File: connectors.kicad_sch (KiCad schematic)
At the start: 1 part

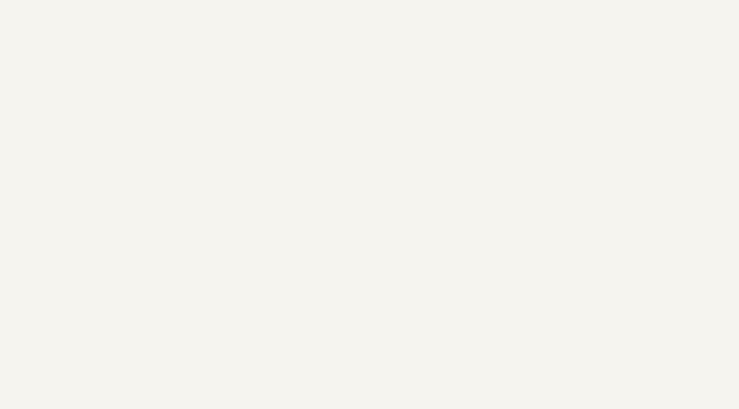
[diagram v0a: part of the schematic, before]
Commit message: Add FAKRA connector
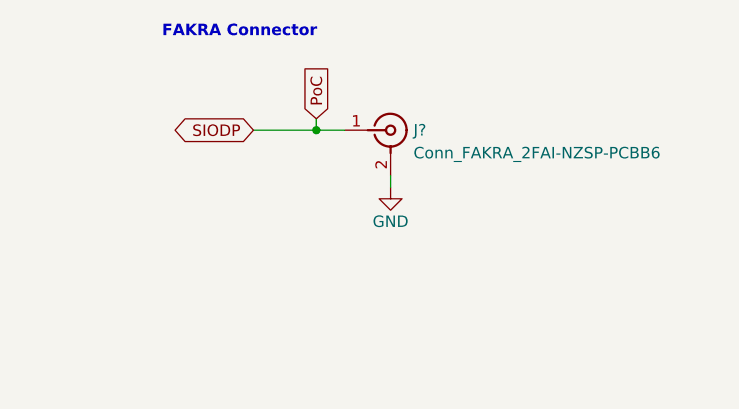
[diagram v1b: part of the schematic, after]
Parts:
- added J?: Conn_FAKRA_2FAI-NZSP-PCBB6, antmicro-footprints:Conn_FAKRA_59S2AQ-40MT5-Z_1, symbol antmicroCoaxialConnectorsRF:Conn_FAKRA_59S2AQ-40MT5-Z_1
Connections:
- net GND: now also J?.2, J?.3, J?.4, J?.5
- new net PoC: J?.1
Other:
- note added: "FAKRA Connector"
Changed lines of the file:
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@@
   (junction (at 58.42 68.58) (diameter 0) (color 0 0 0 0)
+  )
+  (junction (at 230.505 40.64) (diameter 0) (color 0 0 0 0)
   )
   (junction (at 62.23 157.48) (diameter 0) (color 0 0 0 0)
@@
     (stroke (width 0) (type default) (color 0 0 0 0))
   )
+  (wire (pts (xy 230.505 40.64) (xy 233.68 40.64))
+    (stroke (width 0) (type default) (color 0 0 0 0))
+  )
   (wire (pts (xy 52.07 160.02) (xy 62.23 160.02))
     (stroke (width 0) (type default) (color 0 0 0 0))
@@
     (stroke (width 0) (type default) (color 0 0 0 0))
   )
+  (wire (pts (xy 238.76 45.72) (xy 238.76 46.99))
+    (stroke (width 0) (type default) (color 0 0 0 0))
+  )
+  (wire (pts (xy 230.505 39.37) (xy 230.505 40.64))
+    (stroke (width 0) (type default) (color 0 0 0 0))
+  )
   (wire (pts (xy 62.23 157.48) (xy 62.23 160.02))
     (stroke (width 0) (type default) (color 0 0 0 0))
@@
   )
   (wire (pts (xy 52.07 139.7) (xy 64.77 139.7))
+    (stroke (width 0) (type default) (color 0 0 0 0))
+  )
+  (wire (pts (xy 223.52 40.64) (xy 230.505 40.64))
     (stroke (width 0) (type default) (color 0 0 0 0))
   )
@@
     (effects (font (size 1.27 1.27)) (justify left bottom))
   )
+  (text "FAKRA Connector\n" (at 213.36 30.48 0)
+    (effects (font (size 1.27 1.27) (thickness 0.254) bold) (justify left bottom))
+  )
   (text "FFC CSI Connector" (at 38.1 30.48 0)
     (effects (font (size 1.27 1.27) (thickness 0.254) bold) (justify left bottom))
@@
     )
   )
+  (global_label "PoC" (shape input) (at 230.505 39.37 90) (fields_autoplaced)
+    (effects (font (size 1.27 1.27)) (justify left))
+    (property "Intersheet References" "${INTERSHEET_REFS}" (id 0) (at 230.4256 33.2679 90)
+      (effects (font (size 1.27 1.27)) (justify left) hide)
+    )
+  )
   (global_label "CSI0_CLK_N" (shape input) (at 64.77 109.22 0) (fields_autoplaced)
     (effects (font (size 1.27 1.27)) (justify left))
@@
     (property "Intersheet References" "${INTERSHEET_REFS}" (id 0) (at 72.8679 139.6206 0)
       (effects (font (size 1.27 1.27)) (justify left) hide)
+    )
+  )
+  (global_label "SIODP" (shape bidirectional) (at 223.52 40.64 180)
+    (effects (font (size 1.27 1.27)) (justify right))
+    (property "Intersheet References" "${INTERSHEET_REFS}" (id 0) (at 213.36 40.64 0)
+      (effects (font (size 1.27 1.27)) (justify right) hide)
     )
   )
@@
     )
     (pin "1")
+  )
+  (symbol (lib_id "antmicroCoaxialConnectorsRF:Conn_FAKRA_59S2AQ-40MT5-Z_1") (at 233.68 40.64 0) (unit 1)
+    (in_bom yes) (on_board yes)
+    (property "Reference" "J?" (id 0) (at 241.3 40.64 0)
+      (effects (font (size 1.27 1.27) (thickness 0.15)) (justify left))
+    )
+    (property "Value" "Conn_FAKRA_2FAI-NZSP-PCBB6" (id 1) (at 241.3 43.18 0)
+      (effects (font (size 1.27 1.27) (thickness 0.15)) (justify left))
+    )
+    (property "Footprint" "antmicro-footprints:Conn_FAKRA_59S2AQ-40MT5-Z_1" (id 2) (at 254 50.8 0)
+      (effects (font (size 1.27 1.27) (thickness 0.15)) (justify left bottom) hide)
+    )
+    (property "Datasheet" "https://products.rosenberger.com/radio-frequency/connectors/288881/59s2aq-40mt5-z-1-right-angle-plug-pcb-w.-housing" (id 3) (at 254 53.34 0)
+      (effects (font (size 1.27 1.27) (thickness 0.15)) (justify left bottom) hide)
+    )
+    (property "MPN" "59S2AQ-40MT5-Z_1" (id 4) (at 254 55.88 0)
+      (effects (font (size 1.27 1.27) (thickness 0.15)) (justify left bottom) hide)
+    )
+    (property "Manufacturer" "Rosenberger" (id 5) (at 254 58.42 0)
+      (effects (font (size 1.27 1.27) (thickness 0.15)) (justify left bottom) hide)
+    )
+    (property "Author" "Antmicro" (id 6) (at 254 60.96 0)
+      (effects (font (size 1.27 1.27) (thickness 0.15)) (justify left bottom) hide)
+    )
+    (property "License" "Apache-2.0" (id 7) (at 254 63.5 0)
+      (effects (font (size 1.27 1.27) (thickness 0.15)) (justify left bottom) hide)
+    )
+    (pin "1")
+    (pin "2")
+    (pin "3")
+    (pin "4")
+    (pin "5")
   )
   (symbol (lib_id "antmicroFCCConnectors:Conn_FFC_WE_68715014022") (at 52.07 40.64 0) (mirror y) (unit 1)
@@
     (pin "MP2")
   )
+  (symbol (lib_id "antmicropower:GND") (at 238.76 46.99 0) (unit 1)
+    (in_bom yes) (on_board yes)
+    (property "Reference" "#PWR?" (id 0) (at 247.65 49.53 0)
+      (effects (font (size 1.27 1.27) (thickness 0.15)) (justify left bottom) hide)
+    )
+    (property "Value" "GND" (id 1) (at 238.76 50.8 0)
+      (effects (font (size 1.27 1.27) (thickness 0.15)))
+    )
+    (property "Footprint" "" (id 2) (at 247.65 54.61 0)
+      (effects (font (size 1.27 1.27) (thickness 0.15)) (justify left bottom) hide)
+    )
+    (property "Datasheet" "" (id 3) (at 247.65 59.69 0)
+      (effects (font (size 1.27 1.27) (thickness 0.15)) (justify left bottom) hide)
+    )
+    (property "Author" "Antmicro" (id 4) (at 247.65 54.61 0)
+      (effects (font (size 1.27 1.27) (thickness 0.15)) (justify left bottom) hide)
+    )
+    (property "License" "Apache-2.0" (id 5) (at 247.65 57.15 0)
+      (effects (font (size 1.27 1.27) (thickness 0.15)) (justify left bottom) hide)
+    )
+    (pin "1")
+  )
 )

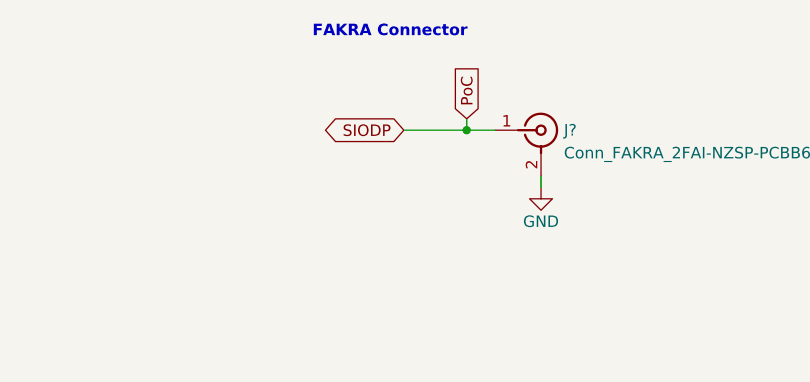
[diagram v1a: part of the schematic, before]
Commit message: [WiP]:Add serializer signals and decoupling capacitors
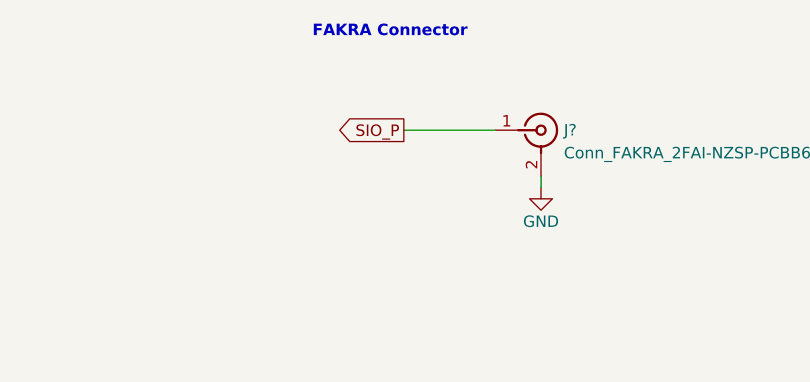
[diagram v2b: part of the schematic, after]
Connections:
- net PoC renamed SIO_P
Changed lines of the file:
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@@
   (junction (at 58.42 68.58) (diameter 0) (color 0 0 0 0)
-  )
-  (junction (at 230.505 40.64) (diameter 0) (color 0 0 0 0)
   )
   (junction (at 62.23 157.48) (diameter 0) (color 0 0 0 0)
@@
     (stroke (width 0) (type default) (color 0 0 0 0))
   )
-  (wire (pts (xy 230.505 40.64) (xy 233.68 40.64))
+  (wire (pts (xy 223.52 40.64) (xy 233.68 40.64))
     (stroke (width 0) (type default) (color 0 0 0 0))
   )
@@
     (stroke (width 0) (type default) (color 0 0 0 0))
   )
-  (wire (pts (xy 230.505 39.37) (xy 230.505 40.64))
-    (stroke (width 0) (type default) (color 0 0 0 0))
-  )
   (wire (pts (xy 62.23 157.48) (xy 62.23 160.02))
     (stroke (width 0) (type default) (color 0 0 0 0))
@@
   )
   (wire (pts (xy 52.07 139.7) (xy 64.77 139.7))
-    (stroke (width 0) (type default) (color 0 0 0 0))
-  )
-  (wire (pts (xy 223.52 40.64) (xy 230.505 40.64))
     (stroke (width 0) (type default) (color 0 0 0 0))
   )
@@
     )
   )
-  (global_label "PoC" (shape input) (at 230.505 39.37 90) (fields_autoplaced)
-    (effects (font (size 1.27 1.27)) (justify left))
-    (property "Intersheet References" "${INTERSHEET_REFS}" (id 0) (at 230.4256 33.2679 90)
-      (effects (font (size 1.27 1.27)) (justify left) hide)
-    )
-  )
   (global_label "CSI0_CLK_N" (shape input) (at 64.77 109.22 0) (fields_autoplaced)
     (effects (font (size 1.27 1.27)) (justify left))
@@
     )
   )
+  (global_label "SIO_P" (shape output) (at 223.52 40.64 180) (fields_autoplaced)
+    (effects (font (size 1.27 1.27)) (justify right))
+    (property "Intersheet References" "${INTERSHEET_REFS}" (id 0) (at 215.7245 40.5606 0)
+      (effects (font (size 1.27 1.27)) (justify right) hide)
+    )
+  )
   (global_label "SDA_0" (shape input) (at 64.77 137.16 0) (fields_autoplaced)
     (effects (font (size 1.27 1.27)) (justify left))
@@
     )
   )
-  (global_label "SIODP" (shape bidirectional) (at 223.52 40.64 180)
-    (effects (font (size 1.27 1.27)) (justify right))
-    (property "Intersheet References" "${INTERSHEET_REFS}" (id 0) (at 213.36 40.64 0)
-      (effects (font (size 1.27 1.27)) (justify right) hide)
-    )
-  )

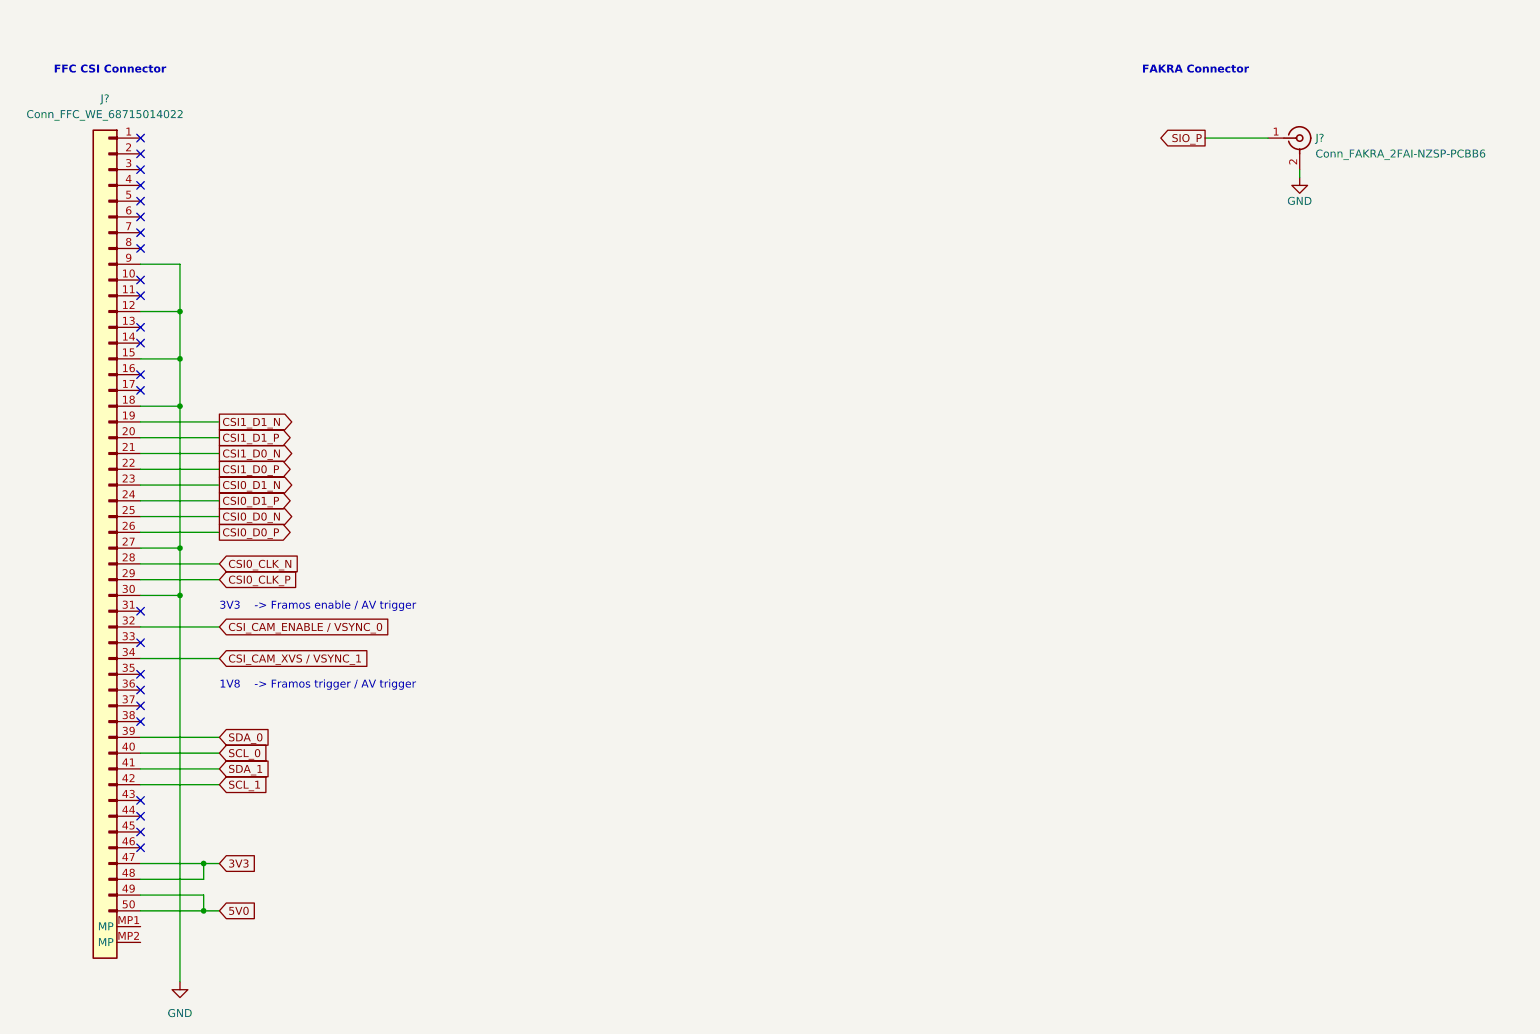
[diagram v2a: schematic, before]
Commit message: Add i2c and gpio triggers
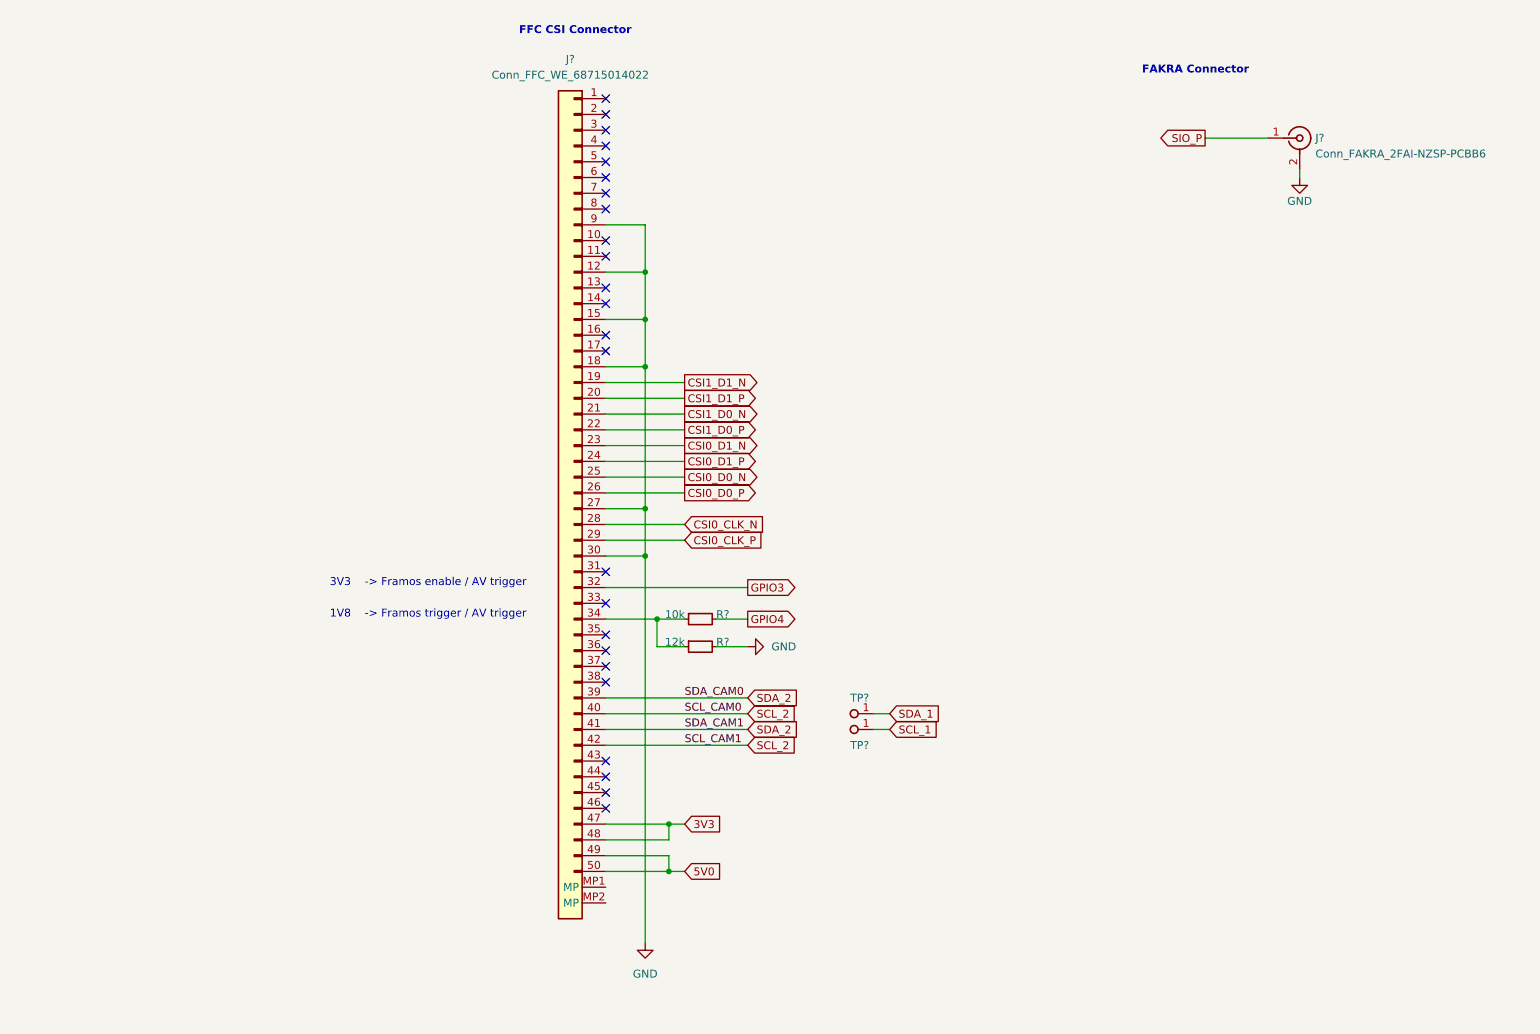
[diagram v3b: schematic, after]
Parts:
- added R?: R_10k_0402, framos-csi-adapter-footprints:R_0402_1005Metric, symbol framos-csi-adapter:R_10k_0402
- added R?: R_12k_0402, framos-csi-adapter-footprints:R_0402_1005Metric, symbol framos-csi-adapter:R_12k_0402
- added TP? (x2): TP_1.5mm_SMD, antmicro-footprints:TP_SMD_1.5mm, symbol antmicroTestPoints:TP_1.5mm_SMD
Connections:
- net GND: now also R?.2
- net SCL_1: now also TP?.1; no longer J?.42
- net SDA_1: now also TP?.1; no longer J?.41
- net CSI_CAM_ENABLE / VSYNC_0 renamed GPIO3
- net CSI_CAM_XVS / VSYNC_1: no longer names the net of J?.34
- net CSI_CAM_XVS / VSYNC_1: now also R?.1, R?.1
- net SCL_0 renamed SCL_2
- net SCL_2: now also J?.42
- net SDA_0 renamed SDA_2
- net SDA_2: now also J?.41
- new net GPIO4: R?.2
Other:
- moved on the sheet: J?
